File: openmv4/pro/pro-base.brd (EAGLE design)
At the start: 35.6 x 44.5 mm, 158 parts, among them J2 SAMTEC_FTSH-105-01-F-DVSAMTEC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, J6 2337019-1, M1 9774030243R, M2 9774030243R, Q1 BSS138, Q2 AO3401, U1 W25Q256JVEIQ_TR, U10 STM32H743IIK6, U11 TEXAS_INSTRUMENTS_BQ24072TRGT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, U14 IS42S32800, U2 EMIF06-MSD02N16, U3 ME6211C18M5G, U4 PAM2305AABADJ, U5 LSM6DS3TR-C, U6 MICROCHIP_USB3320C-EZK-TRMICR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, U7 LBEE5KL1DX-TEMP, U8 STMICROELECTRONICS_VL53L1CXV0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, U9 NXP_SEMICONDUCTORS_SE050C2HQ1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, X2 USD-1040310811, X3 DF12-36-DS, X4 S2B-PH-K-S(LF)(SN), Y0 SITIME_SIT1533AI-H4-DCC-32.76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, Y1 DSC1001BI1-024.0000

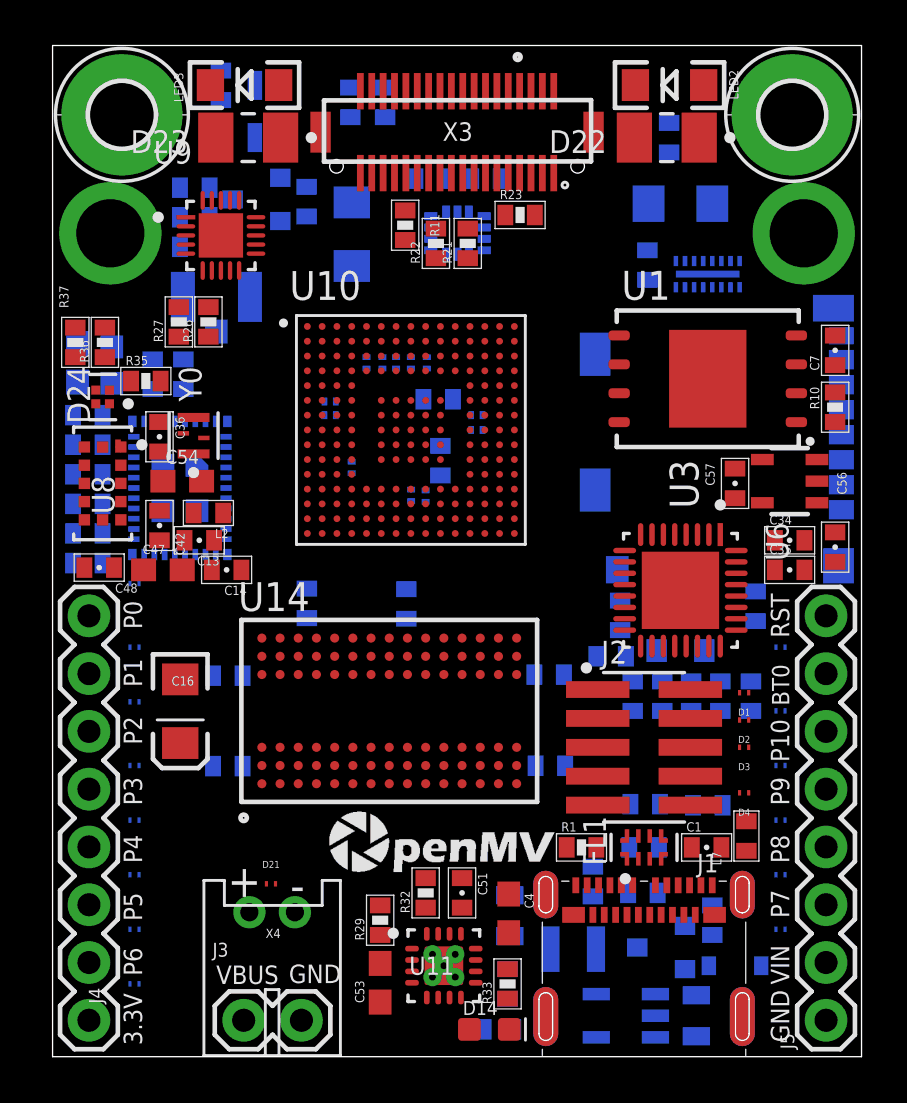
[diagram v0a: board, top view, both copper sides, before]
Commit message: Fix wifi power and tof location
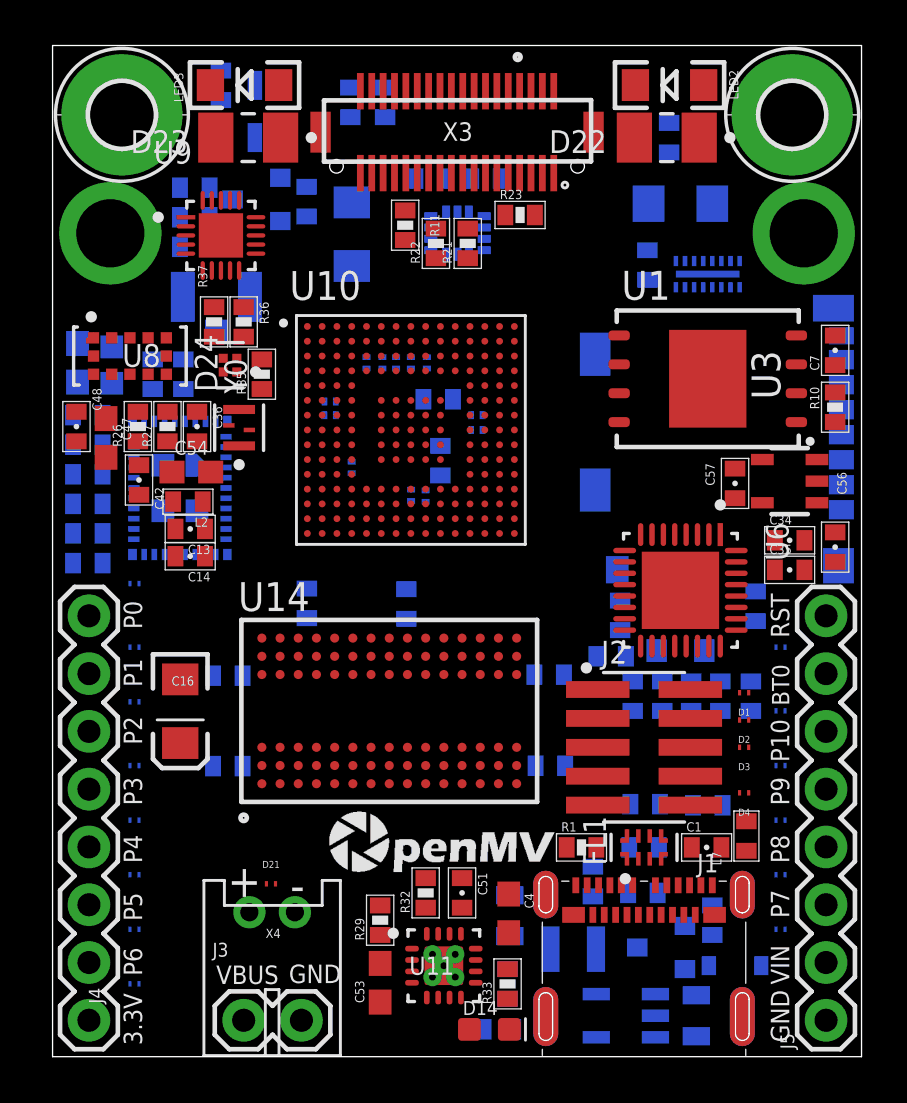
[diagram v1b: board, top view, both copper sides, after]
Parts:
- moved C47 6.32 mm to (2.35, 27.2), turned to 270 degrees
- moved C48 6.28 mm to (1.05, 27.7), turned to 270 degrees
- moved R36 6.17 mm to (8.40, 32.3), turned to 270 degrees
- moved R37 6.17 mm to (7.10, 32.3)
- moved D24 5.77 mm to (7.80, 30.4)
- moved U8 5.73 mm to (3.40, 30.8), turned to 180 degrees
- moved R26 5.55 mm to (3.75, 27.7)
- moved R35 5.11 mm to (9.20, 30.0), turned to 90 degrees
- moved R27 4.63 mm to (5.05, 27.7)
- moved C42 2.19 mm to (3.80, 25.4)
- moved Y0 2.03 mm to (8.20, 27.6)
- moved C36 1.71 mm to (6.35, 27.7)
- moved C14 1.71 mm to (6.05, 22.0)
- moved L2 1.03 mm to (5.95, 24.4)
- moved C13 0.64 mm to (6.05, 23.2)
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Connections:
- removed net 3V3: C38.1, C41.1, C42.1, C54.1, R14.2, R15.2, R16.2, R17.2, R9.2, U7.30, U7.36
- net VCC: now also C38.1, C41.1, C42.1, C54.1, R14.2, R15.2, R16.2, R17.2, R9.2, U7.30, U7.36

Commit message: Update pro
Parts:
- removed J6: 2337019-1, HIROSE - U.FL-R-SMT-1(10):HIROSE_U_FL-R-SMT-1_10_0
- added ANT1: 2450AT18B100E, 2450AT18B100E:ANT_2450AT18B100E
- added C39, C40, C55, C58, C59, C60, C61, C62, C63: 0.1uF, rcl:C0201
- added C64, C65: 4.7uF, SparkFun-Capacitors:0603
- added C66, C67: 1.2pf, sfe:0402-CAP
- added J7: MURATA_MM8130-2600RA2MURATA_MM8130-2600RA2_0_0, Murata - MM8130-2600RA2:MURATA_MM8130-2600RA2_0
- added L4: 3.3nH, SparkFun-Coils:0402
- added R38: 220, sfe:0402-RES
- C26, C27, C28, C29, C30: device sfe:0402-CAP -> rcl:C0201
- moved C7 11.3 mm to (24.7, 25.2), turned to 270 degrees
- moved C30 10.2 mm to (17.2, 16.4), turned to 270 degrees
- moved C29 9.93 mm to (12.0, 12.0), turned to 0 degrees
- moved L3 2.79 mm to (5.30, 29.7), turned to 0 degrees
- moved C41 2.70 mm to (6.65, 31.5), flipped to the top, turned to 270 degrees
- moved R4 2.09 mm to (11.2, 35.5)
- moved C27 1.55 mm to (9.20, 16.4), turned to 270 degrees
- moved C26 1.46 mm to (20.4, 16.4), turned to 270 degrees
- moved C52 1.28 mm to (2.10, 29.7), turned to 0 degrees
- moved R36 1.28 mm to (9.40, 31.5)
- moved C38 1.20 mm to (6.65, 29.2), flipped to the top
- moved C28 1.17 mm to (10.8, 18.8)
- moved R37 1.13 mm to (7.90, 31.5)
- moved U8 0.98 mm to (3.00, 29.9)
- moved R35 0.82 mm to (9.40, 29.2)
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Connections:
- removed net ANT: J6.1, U7.41
- new net ANT_PI_I: C66.1, L4.1, U7.41
- new net ANT_PI_O: C67.1, J7.1, L4.2
- new net LED_IR_INT: Q1.1, R38.2
- new net N$1: ANT1.1, J7.2
- net GND: now also C39.2, C40.2, C55.2, C58.2, C59.2, C60.2, C61.2, C62.2, C63.2, C64.1, C65.1, C66.2, C67.2, J7.3, J7.4, J7.5, J7.6; no longer J6.2, J6.3
- net LED_IR: now also R38.1; no longer Q1.1
- net VCC: now also C39.1, C40.1, C55.1, C58.1, C59.1, C60.1, C61.1, C62.1, C63.1, C64.2, C65.2

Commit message: Update design
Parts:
- added C68: 0.1uF, sfe:0402-CAP
- added U12: MICROCHIP_ATECC608A-SSHDA-BMICROCHIP_ATECC608A-SSHDA-B_0_0, Microchip - ATECC608A-SSHDA-B:MICROCHIP_ATECC608A-SSHDA-B_0
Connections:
- net GND: now also C68.2, U12.4
- net I2C4_SCL: now also U12.6
- net I2C4_SDA: now also U12.5
- net VCC: now also C68.1, U12.8

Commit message: Fix pin naming
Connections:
- net DCMI_D5: now also U10.D11
- net DRAM_D5: no longer U10.D11
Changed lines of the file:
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@@
 <signal name="DCMI_D5" class="5">
 <contactref element="X3" pad="33"/>
+<contactref element="U10" pad="D11"/>
+<wire x1="17.7" y1="30.15" x2="14.03" y2="38.8399" width="0" layer="19" extent="1-1"/>
 </signal>
 <signal name="DCMI_D6" class="5">
@@
 <contactref element="U14" pad="M8"/>
 <contactref element="U10" pad="P8"/>
-<contactref element="U10" pad="D11"/>
-<wire x1="15.75" y1="23.65" x2="17.7" y2="30.15" width="0" layer="19" extent="1-1"/>
 <wire x1="18" y1="17.6" x2="15.75" y2="23.65" width="0" layer="19" extent="1-1"/>
 </signal>

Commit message: Remove NXP chip
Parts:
- removed C49, C50: 0.1uF, sfe:0402-CAP
- removed R28: 100K, sfe:0402-RES
- removed U9: NXP_SEMICONDUCTORS_SE050C2HQ1-Z01SDZNXP_SEMICONDUCTORS_SE05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, Z01SDZ:NXP_SEMICONDUCTORS_SE050C2HQ1-Z01SDZ_1
- moved U12 18.4 mm to (8.70, 35.9)
- moved C68 17.8 mm to (4.80, 32.4), turned to 180 degrees
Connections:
- net CRYPTOEN: no longer R28.2, U9.11
- net GND: no longer C49.2, C50.2, R28.1, U9.1, U9.17, U9.19, U9.21
- net I2C4_SCL: no longer U9.10
- net I2C4_SDA: no longer U9.9
- net VCC: no longer C49.1, C50.1, U9.12, U9.13, U9.14, U9.15, U9.16, U9.18, U9.3

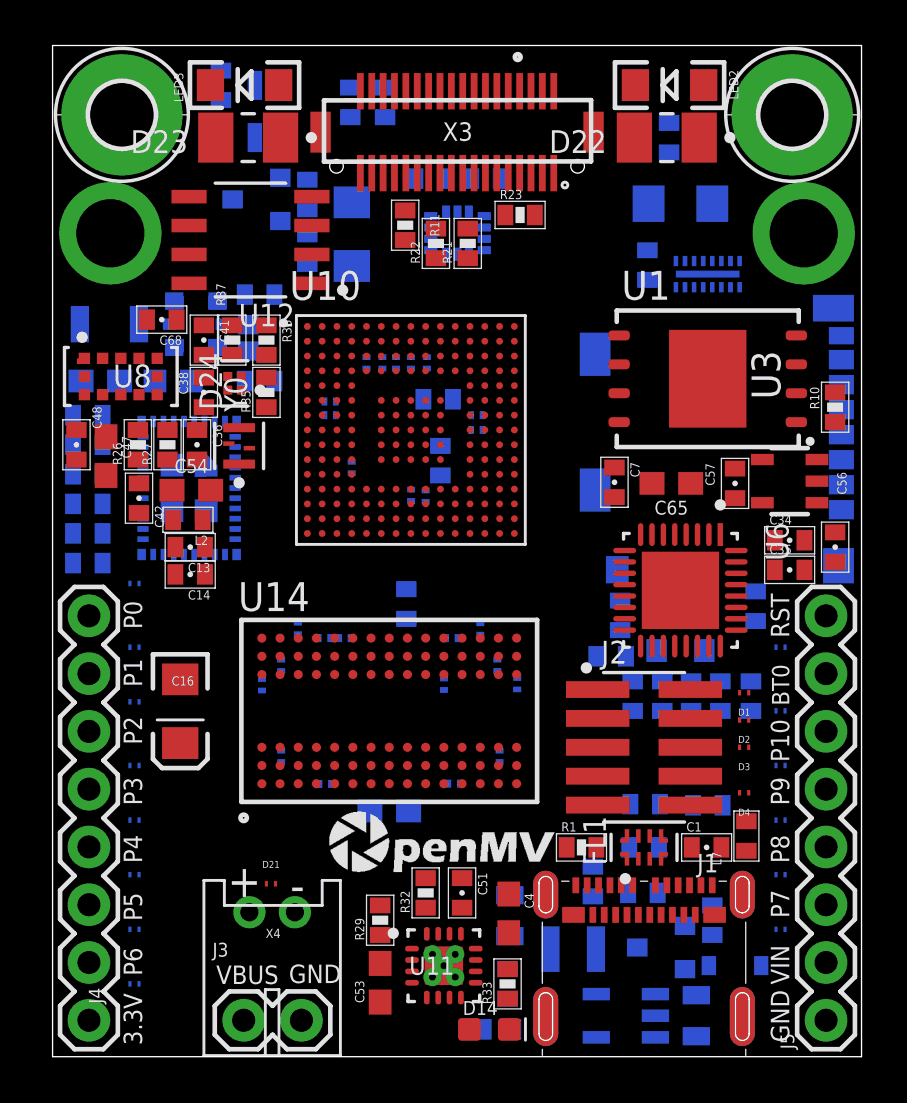
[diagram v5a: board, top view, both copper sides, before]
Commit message: Update the Pro witht he 8x8 ToF
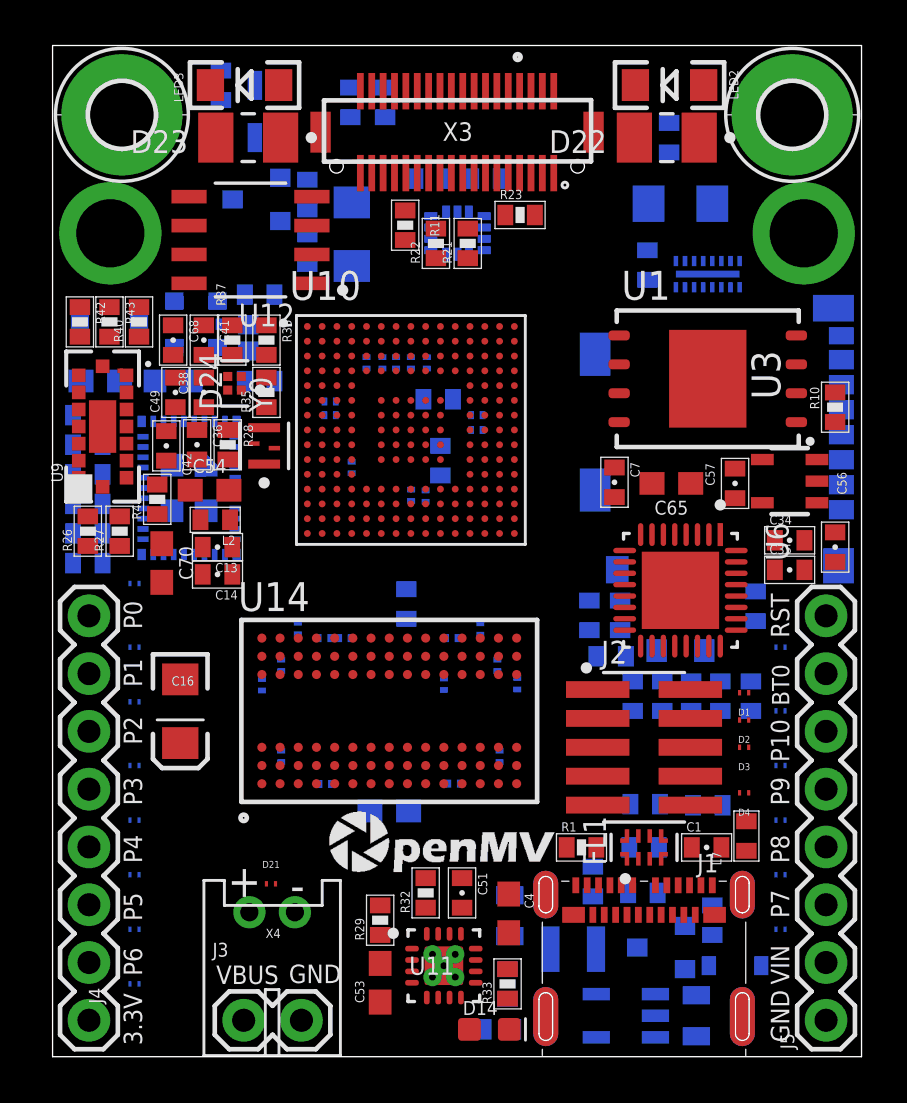
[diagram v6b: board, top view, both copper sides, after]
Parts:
- removed C47: 4.7uF, SparkFun-Capacitors:0603
- removed C48: 0.1uF, sfe:0402-CAP
- removed U8: STMICROELECTRONICS_VL53L1CXV0FY-1STMICROELECTRONICS_VL53L1C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, STMicroelectronics - VL53L1CXV0FY:STMICROELECTRONICS_VL53L1CXV0FY-1_0
- added C49: 0.1uF, sfe:0402-CAP
- added C70: 4.7uF, SparkFun-Capacitors:0603
- added R28, R39: 0, sfe:0402-RES
- added R40, R41, R42, R43: 47K, sfe:0402-RES
- added U9: VL53L5CX, SparkFun-Sensors:VL53L5CX
- moved R26 4.39 mm to (1.55, 23.1)
- moved R27 4.34 mm to (2.95, 23.1)
- moved C42 2.59 mm to (5.00, 26.9)
- moved C13 1.20 mm to (7.25, 22.4)
- moved C14 1.20 mm to (7.25, 21.2)
- moved L2 1.20 mm to (7.15, 23.6)
- moved Y0 1.10 mm to (9.30, 26.9)
- moved C68 1.03 mm to (5.30, 31.5), turned to 270 degrees
- moved C54 0.80 mm to (6.90, 24.9)
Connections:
- removed net CRYPTOEN: U10.L15
- new net I2C_RST: R40.1, U10.L15, U9.A1
- new net N$2: R28.1, U7.37
- new net N$3: R39.1, U6.26
- new net N$5: R41.2, U9.A5
- new net N$6: R42.2, U9.C2
- new net N$7: R43.2, U9.A3
- net 24MHZ_CLK: now also R39.2; no longer U6.26
- net 32.768KHZ_CLK: now also R28.2; no longer U7.37
- net GND: now also C49.2, C70.1, R40.2, U9.A2, U9.A6, U9.A7, U9.B4, U9.C1, U9.C6, U9.C7; no longer C47.2, C48.2, U8.12, U8.2, U8.3, U8.4, U8.6
- net I2C4_SCL: now also U9.C4; no longer U8.10
- net I2C4_SDA: now also U9.C3; no longer U8.9
- net VCC: now also C49.1, C70.2, R41.1, R42.1, R43.1, U9.A4, U9.B1, U9.B7; no longer C47.1, C48.1, U8.1, U8.11, U8.5

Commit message: Update pro design with fixes
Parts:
- removed ANT1: 2450AT18B100E, 2450AT18B100E:ANT_2450AT18B100E
- removed C66, C67: 1.2pf, sfe:0402-CAP
- removed J7: MURATA_MM8130-2600RA2MURATA_MM8130-2600RA2_0_0, Murata - MM8130-2600RA2:MURATA_MM8130-2600RA2_0
- removed L4: 3.3nH, SparkFun-Coils:0402
- added J6: RSP-122811-01, RSP-122811-01:SAMTEC_RSP-122811-01
- added R44: 1.18K, sfe:0402-RES
- added R45: 46.4K, sfe:0402-RES
- JP2: value JUMPER-SMT_2_NC_PASTE_SILK -> JUMPER-SMT_2_NO_SILK; device SparkFun-Jumpers:SMT-JUMPER_2_NC_PASTE_SILK -> SparkFun-Jumpers:SMT-JUMPER_2_NO_SILK
- R32: value 1.8K -> 1.13K
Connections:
- net CHG_LED renamed N$10
- net P10 renamed FSIN
- removed net ANT_PI_O: C67.1, J7.1, L4.2
- removed net N$1: ANT1.1, J7.2
- new net N$4: R44.2, U11.12
- new net N$8: R45.1, U11.14
- net ANT_PI_I: now also J6.1; no longer C66.1, L4.1
- net GND: now also J6.G1, J6.G2, R44.1, R45.2, U11.6; no longer C66.2, C67.2, J7.3, J7.4, J7.5, J7.6, R19.2, U11.5
- net OUT: now also U11.5; no longer U11.6
- net VCC: now also R19.2
